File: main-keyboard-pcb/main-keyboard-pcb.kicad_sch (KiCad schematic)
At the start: 17 parts

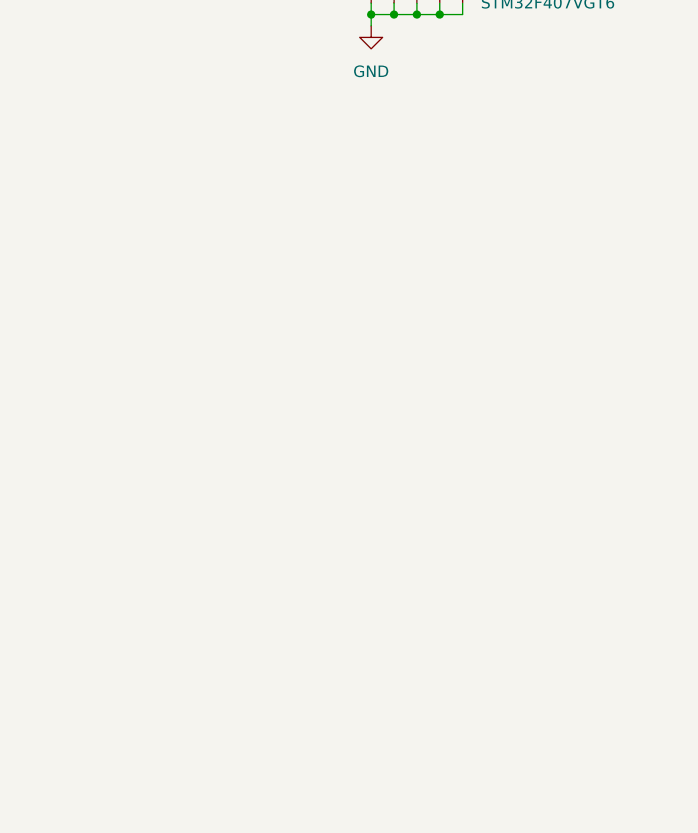
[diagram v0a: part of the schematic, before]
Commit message: Added buck converter to schematic
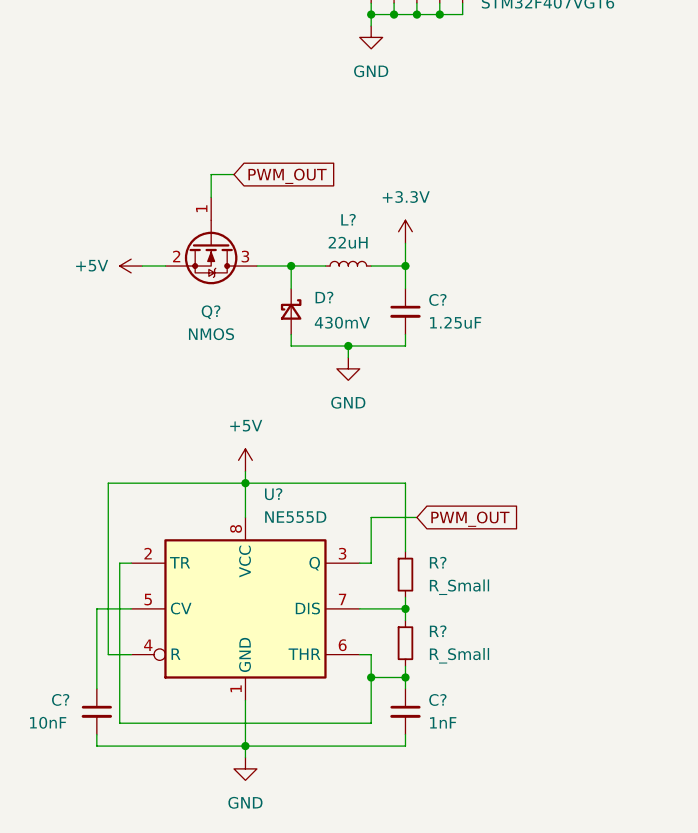
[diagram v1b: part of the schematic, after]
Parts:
- added C?: 1.25uF, symbol Device:C_Small
- added C?: 10nF, symbol Device:C_Small
- added C?: 1nF, symbol Device:C_Small
- added D?: 430mV, symbol Device:D_Schottky_Small
- added L?: 22uH, symbol Device:L_Small
- added Q?: NMOS, symbol Device:Q_NMOS_GSD
- added R? (x2): R_Small, symbol Device:R_Small
- added U?: NE555D, Package_SO:SOIC-8_3.9x4.9mm_P1.27mm, symbol Timer:NE555D
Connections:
- net +3.3V: now also C?.1, L?.2
- net GND: now also C?.2, C?.2, C?.2, D?.2 (A), U?.1 (GND)
- new net: D?.1 (K), L?.1, Q?.3 (D)
- new net: R?.1, R?.2, U?.7 (DIS)
- new net: C?.1, R?.2, U?.2 (TR), U?.6 (THR)
- new net: C?.1, U?.5 (CV)
- new net +5V: Q?.2 (S), R?.1, U?.4 (R), U?.8 (VCC)
- new net PWM_OUT: Q?.1 (G), U?.3 (Q)

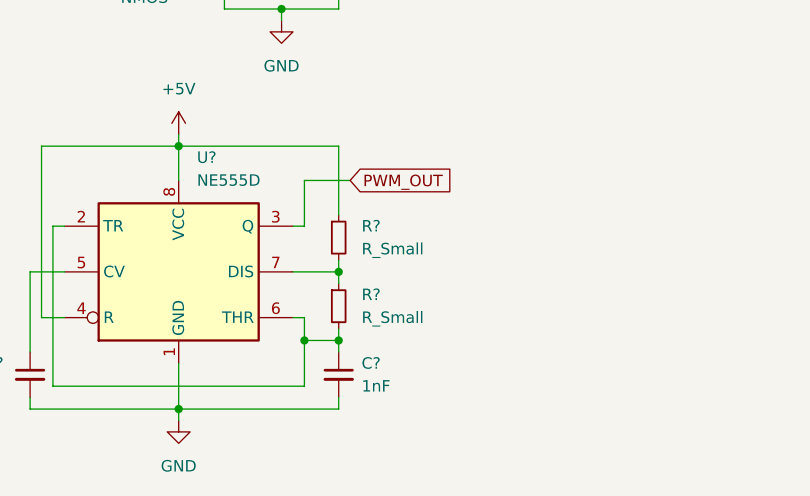
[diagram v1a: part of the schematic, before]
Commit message: Added buck converter footprints
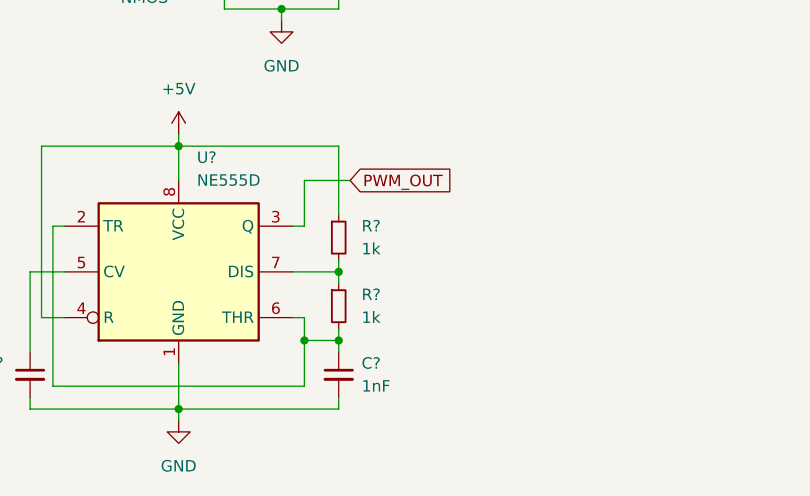
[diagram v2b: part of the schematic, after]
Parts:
- C?: footprint (none) -> buck-converter:C2012X7R1H155K125AC
- C?: footprint (none) -> buck-converter:0402ZC103KAT2A
- C?: footprint (none) -> buck-converter:EMK021BJ102MK-W
- D?: footprint (none) -> buck-converter:RBE1KA20ATR
- L?: footprint (none) -> buck-converter:SRP1038WA220M
- Q?: footprint (none) -> buck-converter:BSS214NWH6327XTSA1
- R? (x2): value R_Small -> 1k; footprint (none) -> buck-converter:ERJ-UP3D1001V
- U?: footprint Package_SO:SOIC-8_3.9x4.9mm_P1.27mm -> buck-converter:NE555D
- U?: footprint Package_QFP:LQFP-100_14x14mm_P0.5mm -> stm32f4:QFP50P1600X1600X160-100N
- Y?: footprint (none) -> stm32f4:ECS-160-10-30B-CKM-TR
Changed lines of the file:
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@@
     (property "Reference" "Q?" (id 0) (at 38.1 222.25 90))
     (property "Value" "NMOS" (id 1) (at 38.1 224.79 90))
-    (property "Footprint" "" (id 2) (at 40.64 219.71 0)
+    (property "Footprint" "buck-converter:BSS214NWH6327XTSA1" (id 2) (at 40.64 219.71 0)
       (effects (font (size 1.27 1.27)) hide)
     )
@@
       (effects (font (size 1.27 1.27)) (justify left))
     )
-    (property "Footprint" "" (id 2) (at 59.69 222.25 0)
+    (property "Footprint" "buck-converter:C2012X7R1H155K125AC" (id 2) (at 59.69 222.25 0)
       (effects (font (size 1.27 1.27)) hide)
     )
@@
       (effects (font (size 1.27 1.27)) (justify left))
     )
-    (property "Footprint" "" (id 2) (at 46.99 222.25 90)
+    (property "Footprint" "buck-converter:RBE1KA20ATR" (id 2) (at 46.99 222.25 90)
       (effects (font (size 1.27 1.27)) hide)
     )
@@
       (effects (font (size 1.27 1.27)) (justify left))
     )
-    (property "Value" "R_Small" (id 1) (at 62.23 252.7299 0)
-      (effects (font (size 1.27 1.27)) (justify left))
-    )
-    (property "Footprint" "" (id 2) (at 59.69 251.46 0)
+    (property "Value" "1k" (id 1) (at 62.23 252.7299 0)
+      (effects (font (size 1.27 1.27)) (justify left))
+    )
+    (property "Footprint" "buck-converter:ERJ-UP3D1001V" (id 2) (at 59.69 251.46 0)
       (effects (font (size 1.27 1.27)) hide)
     )
@@
     (property "Reference" "L?" (id 0) (at 53.34 212.09 90))
     (property "Value" "22uH" (id 1) (at 53.34 214.63 90))
-    (property "Footprint" "" (id 2) (at 53.34 217.17 0)
+    (property "Footprint" "buck-converter:SRP1038WA220M" (id 2) (at 53.34 217.17 0)
       (effects (font (size 1.27 1.27)) hide)
     )
@@
     (property "Reference" "Y?" (id 0) (at 102.87 72.39 0))
     (property "Value" "16MHz" (id 1) (at 102.87 74.93 0))
-    (property "Footprint" "" (id 2) (at 102.87 81.28 0)
+    (property "Footprint" "stm32f4:ECS-160-10-30B-CKM-TR" (id 2) (at 102.87 81.28 0)
       (effects (font (size 1.27 1.27)) hide)
     )
@@
       (effects (font (size 1.27 1.27)) (justify left))
     )
-    (property "Value" "R_Small" (id 1) (at 62.23 260.3499 0)
-      (effects (font (size 1.27 1.27)) (justify left))
-    )
-    (property "Footprint" "" (id 2) (at 59.69 259.08 0)
+    (property "Value" "1k" (id 1) (at 62.23 260.3499 0)
+      (effects (font (size 1.27 1.27)) (justify left))
+    )
+    (property "Footprint" "buck-converter:ERJ-UP3D1001V" (id 2) (at 59.69 259.08 0)
       (effects (font (size 1.27 1.27)) hide)
     )
@@
       (effects (font (size 1.27 1.27)) (justify left))
     )
-    (property "Footprint" "Package_SO:SOIC-8_3.9x4.9mm_P1.27mm" (id 2) (at 63.5 265.43 0)
+    (property "Footprint" "buck-converter:NE555D" (id 2) (at 63.5 265.43 0)
       (effects (font (size 1.27 1.27)) hide)
     )
@@
       (effects (font (size 1.27 1.27)) (justify left))
     )
-    (property "Footprint" "" (id 2) (at 25.4 266.7 0)
+    (property "Footprint" "buck-converter:0402ZC103KAT2A" (id 2) (at 25.4 266.7 0)
       (effects (font (size 1.27 1.27)) hide)
     )
@@
       (effects (font (size 1.27 1.27)) (justify left))
     )
-    (property "Footprint" "" (id 2) (at 59.69 266.7 0)
+    (property "Footprint" "buck-converter:EMK021BJ102MK-W" (id 2) (at 59.69 266.7 0)
       (effects (font (size 1.27 1.27)) hide)
     )
@@
       (effects (font (size 1.27 1.27)) (justify left))
     )
-    (property "Footprint" "Package_QFP:LQFP-100_14x14mm_P0.5mm" (id 2) (at 43.18 182.88 0)
+    (property "Footprint" "stm32f4:QFP50P1600X1600X160-100N" (id 2) (at 43.18 182.88 0)
       (effects (font (size 1.27 1.27)) (justify right) hide)
     )
@@
     )
     (path "/2627ec77-edb8-43a6-a715-3e8643e0ab85"
-      (reference "C?") (unit 1) (value "1.25uF") (footprint "")
+      (reference "C?") (unit 1) (value "1.25uF") (footprint "buck-converter:C2012X7R1H155K125AC")
     )
     (path "/29df8302-65c4-48c9-b422-efae8bd18b0e"
@@
     )
     (path "/dcfdccec-27af-491b-a987-81026dcd4ce4"
-      (reference "C?") (unit 1) (value "10nF") (footprint "")
+      (reference "C?") (unit 1) (value "10nF") (footprint "buck-converter:0402ZC103KAT2A")
     )
     (path "/f1dbd420-a1b8-4df8-bcbf-08e34484c10e"
-      (reference "C?") (unit 1) (value "1nF") (footprint "")
+      (reference "C?") (unit 1) (value "1nF") (footprint "buck-converter:EMK021BJ102MK-W")
     )
     (path "/416758b4-f12a-498f-8dda-4c3e6700d4dd"
-      (reference "D?") (unit 1) (value "430mV") (footprint "")
+      (reference "D?") (unit 1) (value "430mV") (footprint "buck-converter:RBE1KA20ATR")
     )
     (path "/6e9cd9c5-1ae4-4244-ac9e-a6df3f164996"
-      (reference "L?") (unit 1) (value "22uH") (footprint "")
+      (reference "L?") (unit 1) (value "22uH") (footprint "buck-converter:SRP1038WA220M")
     )
     (path "/153bb9c4-742c-4627-aa33-df137a2e7f33"
-      (reference "Q?") (unit 1) (value "NMOS") (footprint "")
+      (reference "Q?") (unit 1) (value "NMOS") (footprint "buck-converter:BSS214NWH6327XTSA1")
     )
     (path "/1498b815-2e1b-4f2c-96b7-e4b7a01905ac"
@@
     )
     (path "/573aea3f-1abb-4d22-ab00-2fec73c525d2"
-      (reference "R?") (unit 1) (value "R_Small") (footprint "")
+      (reference "R?") (unit 1) (value "1k") (footprint "buck-converter:ERJ-UP3D1001V")
     )
     (path "/833e7f42-2bec-42e8-95ff-ff71015aa6f4"
-      (reference "R?") (unit 1) (value "R_Small") (footprint "")
+      (reference "R?") (unit 1) (value "1k") (footprint "buck-converter:ERJ-UP3D1001V")
     )
     (path "/bacba619-35f9-49e7-99a6-9e5be1219a7d"
@@
     )
     (path "/a6493cbf-4cdf-4d05-8dea-172fd36cc489"
-      (reference "U?") (unit 1) (value "NE555D") (footprint "Package_SO:SOIC-8_3.9x4.9mm_P1.27mm")
+      (reference "U?") (unit 1) (value "NE555D") (footprint "buck-converter:NE555D")
     )
     (path "/f1fb2386-fdc4-4690-a4ac-240923fcaa73"
-      (reference "U?") (unit 1) (value "STM32F407VGT6") (footprint "Package_QFP:LQFP-100_14x14mm_P0.5mm")
+      (reference "U?") (unit 1) (value "STM32F407VGT6") (footprint "stm32f4:QFP50P1600X1600X160-100N")
     )
     (path "/80632404-0140-4db5-a8ff-8547eb37fef3"
-      (reference "Y?") (unit 1) (value "16MHz") (footprint "")
-    )
-  )
+      (reference "Y?") (unit 1) (value "16MHz") (footprint "stm32f4:ECS-160-10-30B-CKM-TR")
+    )
+  )

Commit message: Added Arisu keswitch matrix
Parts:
- removed C?: 1.25uF, buck-converter:C2012X7R1H155K125AC, symbol Device:C_Small
- removed C?: 10nF, buck-converter:0402ZC103KAT2A, symbol Device:C_Small
- removed C?: 1nF, buck-converter:EMK021BJ102MK-W, symbol Device:C_Small
- removed D?: 430mV, buck-converter:RBE1KA20ATR, symbol Device:D_Schottky_Small
- removed L?: 22uH, buck-converter:SRP1038WA220M, symbol Device:L_Small
- removed Q?: NMOS, buck-converter:BSS214NWH6327XTSA1, symbol Device:Q_NMOS_GSD
- removed R? (x2): 1k, buck-converter:ERJ-UP3D1001V, symbol Device:R_Small
- removed U?: NE555D, buck-converter:NE555D, symbol Timer:NE555D
- added C16, C9: 20uF, symbol Device:C_Small
- added C3: 4.7uF, symbol Device:C_Small
- added C8: C_Small, symbol Device:C_Small
- added D1, D10, D11, D12, D13, D14, D15, D16, D17, D18, D19, D2, D20, D21, D22, D23, D24, D25, D26, D27, D28, D29, D3, D30, D31, D32, D33, D34, D35, D36, D37, D38, D39, D4, D40, D41, D42, D43, D44, D45, D46, D47, D48, D49, D5, D50, D51, D52, D53, D54, D55, D56, D57, D58, D59, D6, D60, D61, D62, D63, D64, D65, D66, D67, D7, D8, D9: D, Diodes_SMD:D_SOD-123, symbol Device:D
- added IC1: LMR51420XDDCR, buck-converter:LMR51420XDDCR, symbol buck-converter:LMR51420XDDCR
- added L1: 25uH, symbol Device:L_Small
- added R1: 100k, symbol Device:R_Small
- added R2: 22.2k, symbol Device:R_Small
- added SW10, SW11, SW12, SW13, SW14, SW16, SW17, SW18, SW19, SW2, SW20, SW21, SW22, SW23, SW25, SW26, SW27, SW28, SW29, SW30, SW31, SW32, SW33, SW34, SW35, SW36, SW37, SW39, SW40, SW41, SW42, SW43, SW44, SW45, SW46, SW48, SW49, SW50, SW51, SW52, SW53, SW54, SW56, SW57, SW59, SW60, SW62, SW63, SW64, SW65, SW66, SW67, SW68, SW7, SW8, SW9: SW_Push, MX_Switch:SW_Cherry_MX_1.00u_PCB, symbol Switch:SW_Push
- added SW15, SW3, SW47, SW6, SW61: SW_Push, MX_Switch:SW_Cherry_MX_1.50u_PCB, symbol Switch:SW_Push
- added SW24: SW_Push, MX_Switch:SW_Cherry_MX_2.00u_PCB_ReversedStabilizers, symbol Switch:SW_Push
- added SW38: SW_Push, MX_Switch:SW_Cherry_MX_2.75u_PCB_ReversedStabilizers, symbol Switch:SW_Push
- added SW4, SW55: SW_Push, MX_Switch:SW_Cherry_MX_1.75u_PCB, symbol Switch:SW_Push
- added SW5: SW_Push, MX_Switch:SW_Cherry_MX_2.25u_PCB, symbol Switch:SW_Push
- added SW58: SW_Push, MX_Switch:SW_Cherry_MX_2.25u_PCB_ReversedStabilizers, symbol Switch:SW_Push
- U2: renamed from U?; footprint stm32f4:QFP50P1600X1600X160-100N -> stm32f4_2:QFP50P1600X1600X160-100N
- Y1: renamed from Y?; footprint stm32f4:ECS-160-10-30B-CKM-TR -> stm32f4_2:ECS-160-10-30B-CKM-TR
- gave numbers to parts that had none: 15
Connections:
- net +5V: now also C3.1, IC1.3 (VIN), IC1.5 (EN)
- net GND: now also C16.2, C3.2, C9.2, IC1.1 (GND), R2.2
- new net: D19.2 (A), SW20.2
- new net: D7.2 (A), SW8.2
- new net: D23.2 (A), SW24.2
- new net: D29.2 (A), SW30.2
- new net: D55.2 (A), SW56.2
- new net: D32.2 (A), SW33.2
- new net: D5.2 (A), SW6.2
- new net: D57.2 (A), SW58.2
- new net: D9.2 (A), SW10.2
- new net: D54.2 (A), SW55.2
- new net: D14.2 (A), SW15.2
- new net: D58.2 (A), SW59.2
- new net: D13.2 (A), SW14.2
- new net: D67.2 (A), SW68.2
- new net: D60.2 (A), SW61.2
- new net: D34.2 (A), SW35.2
- new net: D6.2 (A), SW7.2
- new net: D17.2 (A), SW18.2
- new net: D49.2 (A), SW50.2
- new net: D46.2 (A), SW47.2
- new net: D35.2 (A), SW36.2
- new net: D15.2 (A), SW16.2
- new net: D48.2 (A), SW49.2
- new net: D53.2 (A), SW54.2
- new net: C16.1, C9.1, L1.2, R1.1
- new net: D25.2 (A), SW26.2
- new net: D51.2 (A), SW52.2
- new net: D11.2 (A), SW12.2
- new net: D44.2 (A), SW45.2
- new net: D65.2 (A), SW66.2
- new net: D39.2 (A), SW40.2
- new net: D63.2 (A), SW64.2
- new net: D40.2 (A), SW41.2
- new net: D10.2 (A), SW11.2
- new net: D41.2 (A), SW42.2
- new net: D2.2 (A), SW3.2
- new net: D18.2 (A), SW19.2
- new net: D66.2 (A), SW67.2
- new net: D61.2 (A), SW62.2
- new net: D16.2 (A), SW17.2
- new net: D56.2 (A), SW57.2
- new net: D3.2 (A), SW4.2
- new net: D37.2 (A), SW38.2
- new net: D52.2 (A), SW53.2
- new net: D64.2 (A), SW65.2
- new net: D8.2 (A), SW9.2
- new net: D43.2 (A), SW44.2
- new net: D4.2 (A), SW5.2
- new net: D45.2 (A), SW46.2
- new net: D28.2 (A), SW29.2
- new net: D50.2 (A), SW51.2
- new net: D42.2 (A), SW43.2
- new net: D30.2 (A), SW31.2
- new net: D36.2 (A), SW37.2
- new net: D33.2 (A), SW34.2
- new net: D21.2 (A), SW22.2
- new net: D20.2 (A), SW21.2
- new net: D24.2 (A), SW25.2
- new net: D27.2 (A), SW28.2
- new net: D12.2 (A), SW13.2
- new net: D22.2 (A), SW23.2
- new net: D26.2 (A), SW27.2
- new net: D62.2 (A), SW63.2
- new net: D38.2 (A), SW39.2
- new net: D1.2 (A), SW2.2
- new net: D31.2 (A), SW32.2
- new net: D59.2 (A), SW60.2
- new net: D47.2 (A), SW48.2
- new net BUCK_CB: C8.1, IC1.6 (CB)
- new net BUCK_FB: IC1.4 (FB), R1.2, R2.1
- new net BUCK_SW: C8.2, IC1.2 (SW), L1.1
- new net col0: SW2.1, SW3.1, SW4.1, SW5.1, SW6.1
- new net col1: SW10.1, SW7.1, SW8.1, SW9.1
- new net col10: SW48.1, SW49.1, SW50.1, SW51.1
- new net col11: SW52.1, SW53.1, SW54.1, SW55.1
- new net col12: SW56.1, SW57.1, SW58.1, SW59.1
- new net col13: SW60.1, SW61.1, SW62.1, SW63.1
- new net col14: SW64.1, SW65.1, SW66.1, SW67.1, SW68.1
- new net col2: SW11.1, SW12.1, SW13.1, SW14.1, SW15.1
- new net col3: SW16.1, SW17.1, SW18.1, SW19.1
- new net col4: SW20.1, SW21.1, SW22.1, SW23.1, SW24.1
- new net col5: SW25.1, SW26.1, SW27.1, SW28.1, SW29.1
- new net col6: SW30.1, SW31.1, SW32.1, SW33.1
- new net col7: SW34.1, SW35.1, SW36.1, SW37.1, SW38.1
- new net col8: SW39.1, SW40.1, SW41.1, SW42.1
- new net col9: SW43.1, SW44.1, SW45.1, SW46.1, SW47.1
- new net row0: D1.1 (K), D10.1 (K), D15.1 (K), D19.1 (K), D24.1 (K), D29.1 (K), D33.1 (K), D38.1 (K), D42.1 (K), D47.1 (K), D51.1 (K), D55.1 (K), D59.1 (K), D6.1 (K), D63.1 (K)
- new net row1: D11.1 (K), D16.1 (K), D2.1 (K), D20.1 (K), D25.1 (K), D30.1 (K), D34.1 (K), D39.1 (K), D43.1 (K), D48.1 (K), D52.1 (K), D56.1 (K), D60.1 (K), D64.1 (K), D7.1 (K)
- new net row2: D12.1 (K), D17.1 (K), D21.1 (K), D26.1 (K), D3.1 (K), D31.1 (K), D35.1 (K), D40.1 (K), D44.1 (K), D49.1 (K), D53.1 (K), D57.1 (K), D65.1 (K), D8.1 (K)
- new net row3: D13.1 (K), D18.1 (K), D22.1 (K), D27.1 (K), D32.1 (K), D36.1 (K), D4.1 (K), D41.1 (K), D45.1 (K), D50.1 (K), D54.1 (K), D61.1 (K), D66.1 (K), D9.1 (K)
- new net row4: D14.1 (K), D23.1 (K), D28.1 (K), D37.1 (K), D46.1 (K), D5.1 (K), D58.1 (K), D62.1 (K), D67.1 (K)
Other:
- note added: "'"
- note added: "+"
- note added: ","
- note added: "."
- note added: "/"
- note added: "1"
- note added: "10"
- note added: "2"
- note added: "3"
- note added: "4"
- note added: "5"
- note added: "6"
- note added: "7"
- note added: "8"
- note added: "9"
- note added: ";"
- note added: "A"
- note added: "ALT"
- note added: "B"
- note added: "BKSP"
- note added: "C"
- note added: "CTRL"
- note added: "D"
- note added: "DOWN"
- note added: "E"
- note added: "ENT"
- note added: "ESC"
- note added: "F"
- note added: "FN"
- note added: "G"
- note added: "H"
- note added: "I"
- note added: "J"
- note added: "K"
- note added: "L"
- note added: "LEFT"
- note added: "M"
- note added: "M1"
- note added: "M2"
- note added: "M3"
- note added: "N"
- note added: "O"
- note added: "P"
- note added: "Q"
- note added: "R"
- note added: "RGHT"
- note added: "S"
- note added: "SHFT"
- note added: "SHIFT"
- note added: "SPC"
- note added: "T"
- note added: "TAB"
- note added: "U"
- note added: "UP"
- note added: "V"
- note added: "W"
- note added: "X"
- note added: "Y"
- note added: "Z"
- note added: "["
- note added: "]"
- note added: "_"
- note added: "`"
- note added: "|"
